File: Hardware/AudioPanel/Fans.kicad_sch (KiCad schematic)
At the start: 10 parts, among them U94 R-78E12-0.5

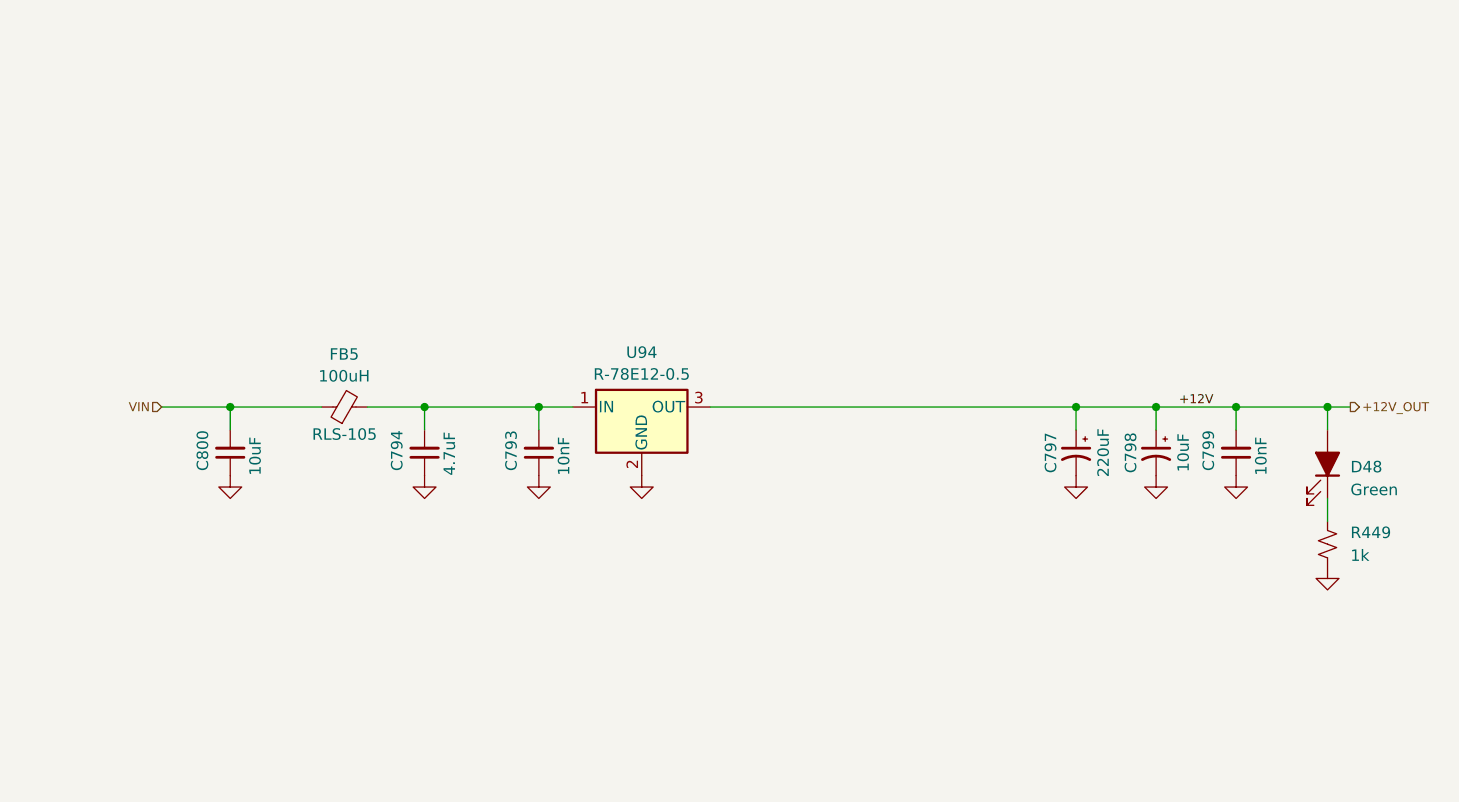
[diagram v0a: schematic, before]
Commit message: Added audio sum amplifiers
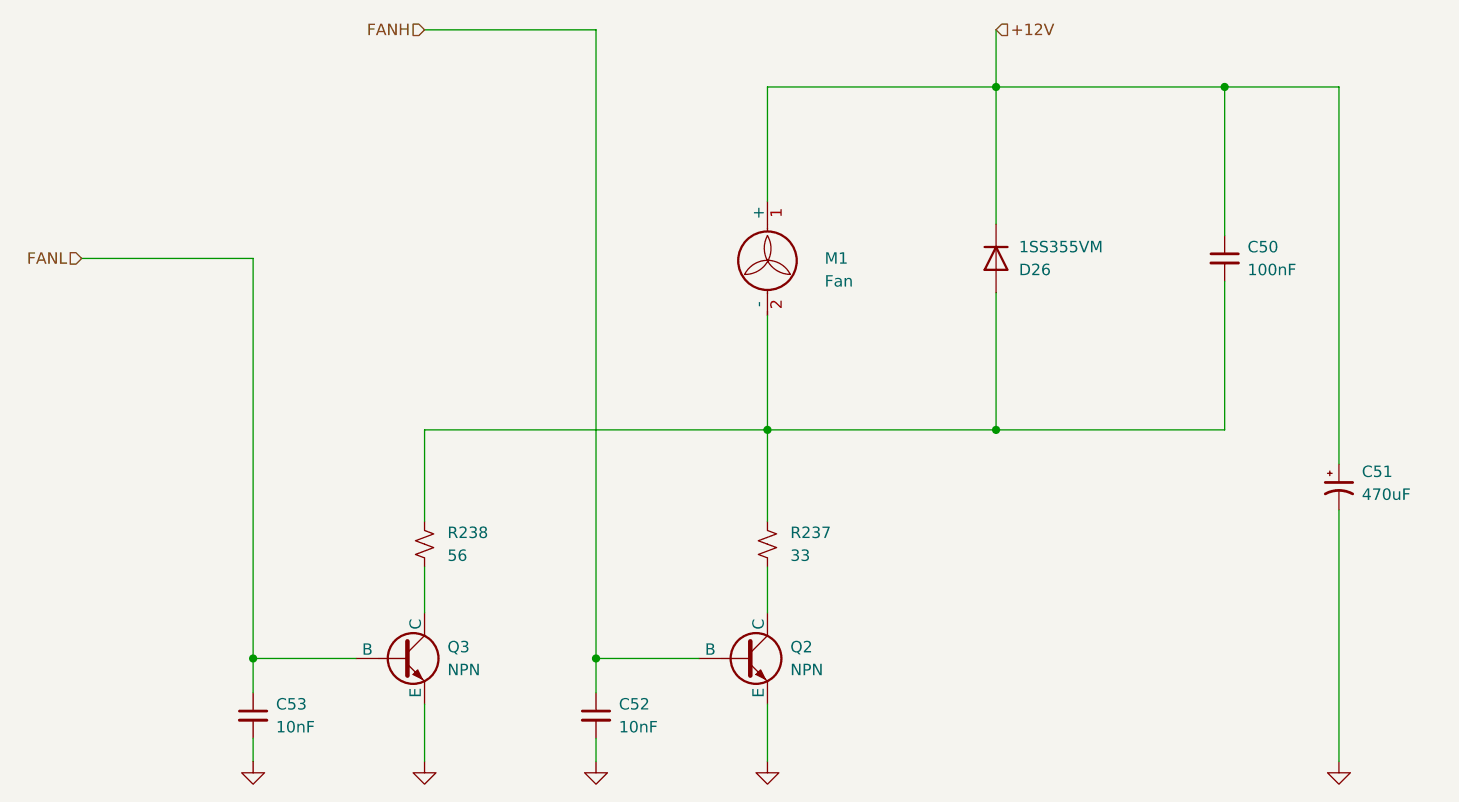
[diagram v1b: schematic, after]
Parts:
- removed C793, C799: 10nF, symbol Device:C_Small
- removed C794: 4.7uF, symbol Device:C_Small
- removed C797: 220uF, symbol Device:C_Polarized_Small_US
- removed C798: 10uF, symbol Device:C_Polarized_Small_US
- removed C800: 10uF, symbol Device:C_Small
- removed D48: Green, LED_THT:LED_D5.0mm, symbol Device:LED_Filled
- removed FB5: 100uH, symbol Device:FerriteBead_Small
- removed R449: 1k, Resistor_SMD:R_0603_1608Metric_Pad0.98x0.95mm_HandSolder, symbol Device:R_Small_US
- removed U94: R-78E12-0.5, Converter_DCDC:Converter_DCDC_RECOM_R-78E-0.5_THT, symbol Regulator_Switching:R-78E12-0.5
- added C50: 100nF, symbol Device:C_Small
- added C51: 470uF, symbol Device:C_Polarized_Small_US
- added C52, C53: 10nF, symbol Device:C_Small
- added D26: 1SS355VM, Diode_SMD:D_SOD-323F, symbol Diode:1SS355VM
- added M1: Fan, symbol Motor:Fan
- added Q2, Q3: NPN, symbol Simulation_SPICE:NPN
- added R237: 33, symbol Device:R_Small_US
- added R238: 56, symbol Device:R_Small_US
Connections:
- net GND: now also C51.2, C52.2, C53.2, Q2.3 (E), Q3.3 (E)
- new net: Q3.1 (C), R238.2
- new net: C50.2, D26.2 (A), M1.2 (-), R237.1, R238.1
- new net: Q2.1 (C), R237.2
- new net +12V: C50.1, C51.1, D26.1 (K), M1.1 (+)
- new net FANH: C52.1, Q2.2 (B)
- new net FANL: C53.1, Q3.2 (B)
